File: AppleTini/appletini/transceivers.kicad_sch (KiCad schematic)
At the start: 22 parts, among them U2 74LS245, U3 74LS245, U4 74LS245, U5 74LS245, U5 74LVC1G07, U6 74LVC1G07, U7 74LVC1G07, U8 74LVC1G07, U9 74LS245

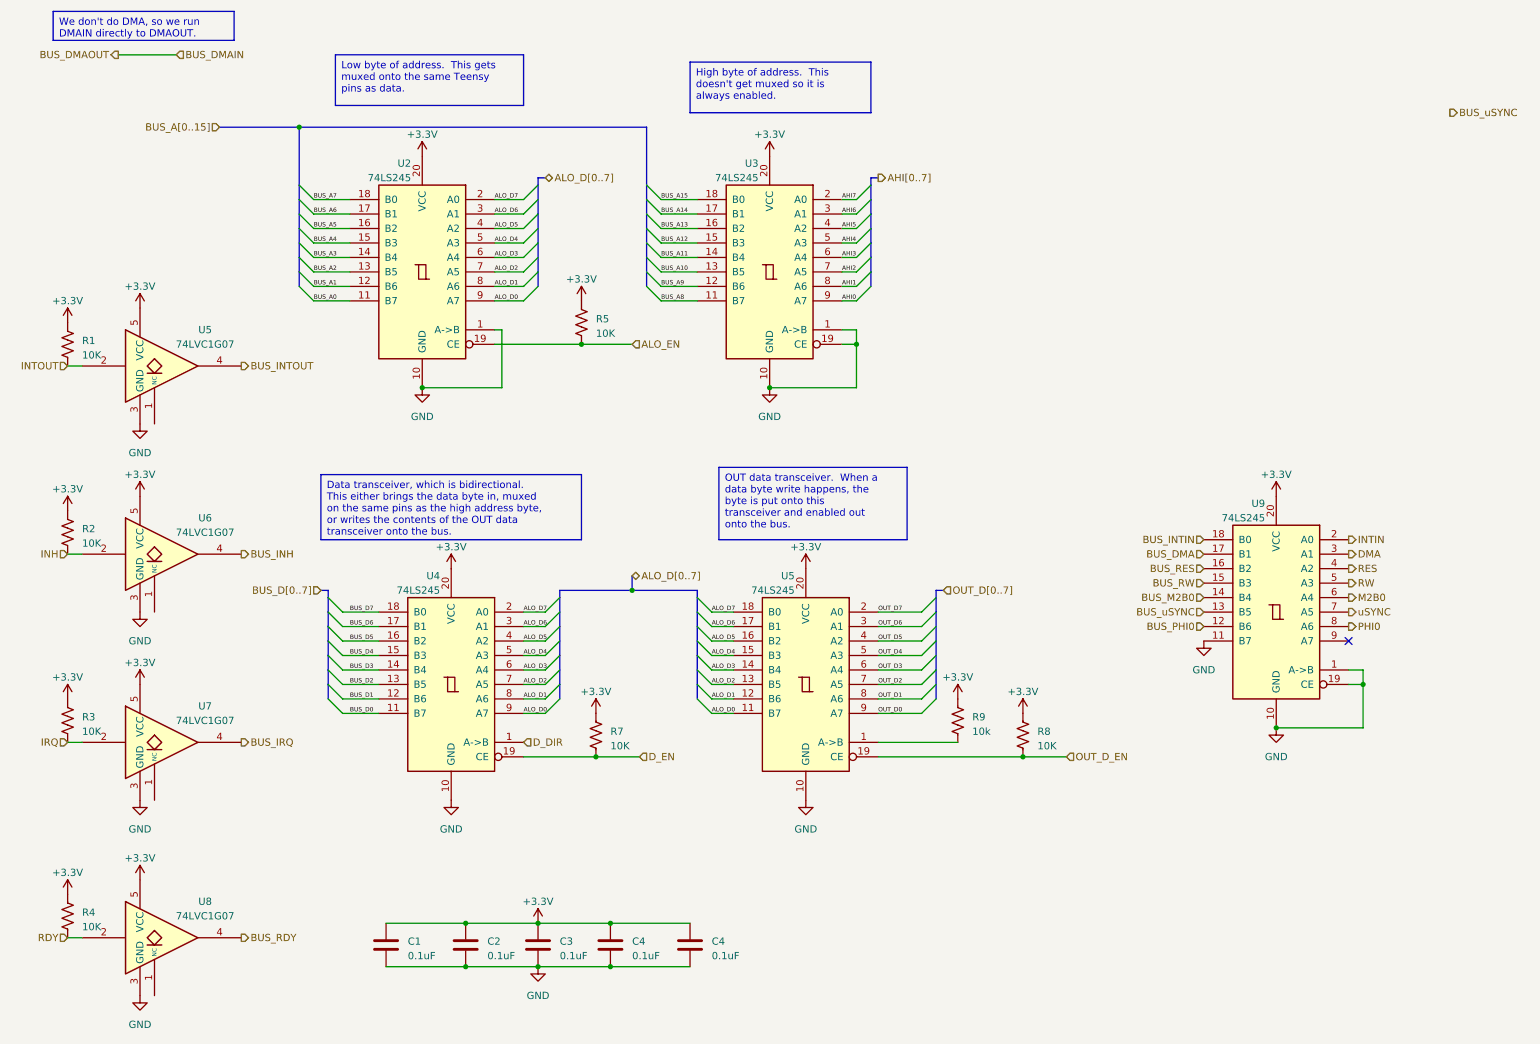
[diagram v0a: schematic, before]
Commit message: Changed to use single LVC07 Shrink vias to 0.6mm Spaced vias further apart Increased zone fill
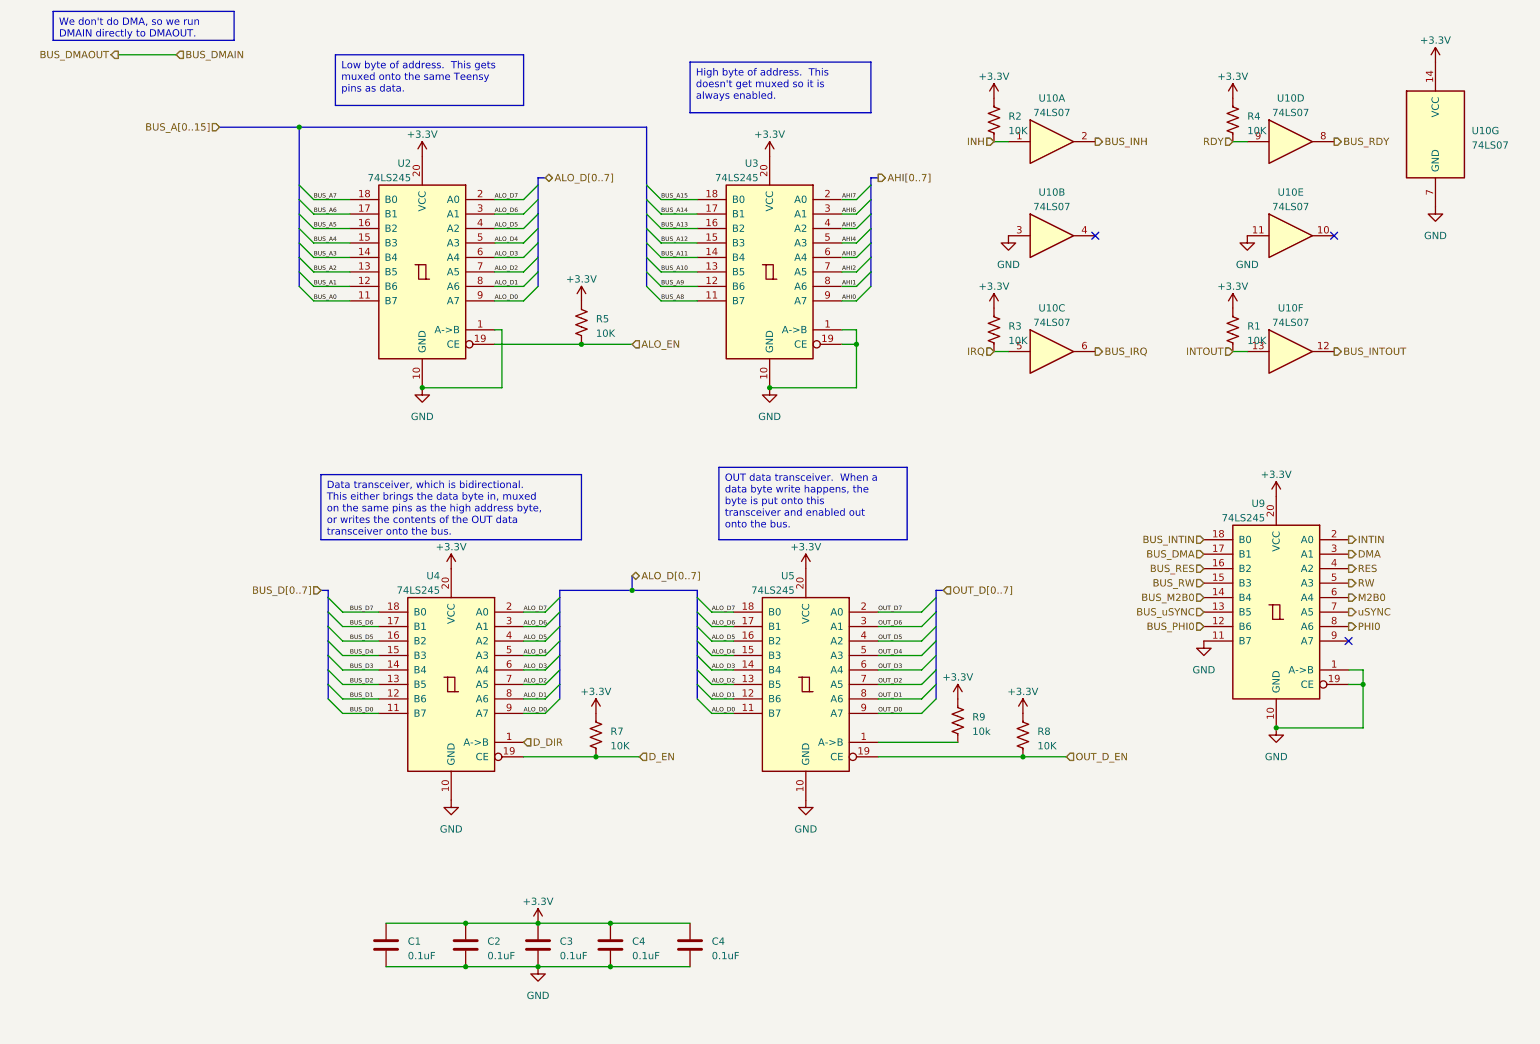
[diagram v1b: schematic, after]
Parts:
- removed U5, U6, U7, U8: 74LVC1G07, Package_TO_SOT_SMD:SOT-23-5, symbol 74xGxx:74LVC1G07
- added U10: 74LS07, Package_SO:TSSOP-14_4.4x5mm_P0.65mm, symbol 74xx:74LS07
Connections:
- net +3.3V: now also U10.14 (VCC)
- net BUS_INH: now also U10.2
- net BUS_INTOUT: now also U10.12
- net BUS_IRQ: now also U10.6
- net BUS_RDY: now also U10.8
- net GND: now also U10.11, U10.3, U10.7 (GND)
- net INH: now also U10.1
- net INTOUT: now also U10.13
- net IRQ: now also U10.5
- net RDY: now also U10.9
- no-connect marks 1 -> 3

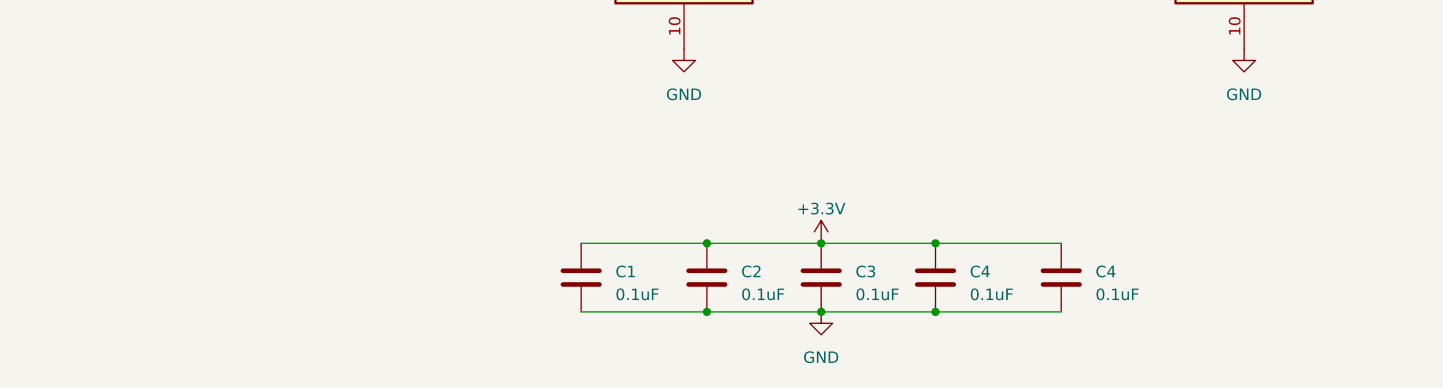
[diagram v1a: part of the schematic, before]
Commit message: Caps on bus power lines
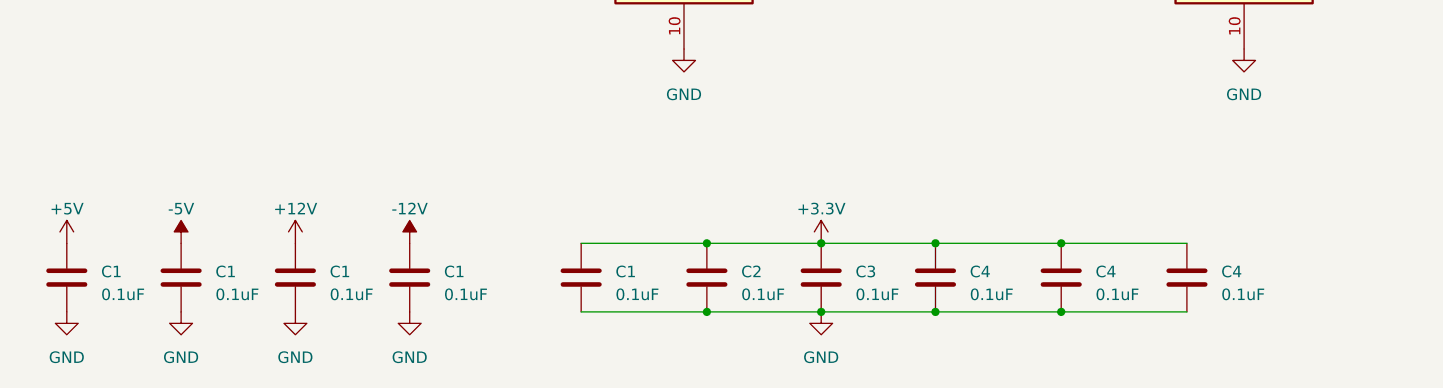
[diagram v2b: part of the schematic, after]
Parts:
- added C1 (x4), C4: 0.1uF, Capacitor_SMD:C_1206_3216Metric, symbol Device:C
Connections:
- net +3.3V: now also C4.1
- net GND: now also C1.2, C1.2, C1.2, C1.2, C4.2
- new net +12V: C1.1
- new net +5V: C1.1
- new net -12V: C1.1
- new net -5V: C1.1

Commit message: part picks and cleanup
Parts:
- C1, C2, C3, C4: LCSC (none) -> C24497
- R1, R2, R3, R4, R5, R7, R8: LCSC (none) -> C2991755
- R9: value 10k -> 10K; LCSC (none) -> C2991755
- U10: LCSC (none) -> C7809
- U2, U3, U4, U5, U9: LCSC (none) -> C6082
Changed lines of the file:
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@@
+      (effects (font (size 1.27 1.27)) hide)
+    )
+    (property "LCSC" "C7809" (at 240.03 74.93 0)
       (effects (font (size 1.27 1.27)) hide)
     )
@@
       (effects (font (size 1.27 1.27)) hide)
     )
+    (property "LCSC" "C6082" (at 154.94 133.35 0)
+      (effects (font (size 1.27 1.27)) hide)
+    )
     (pin "1")
     (pin "10")
@@
       (effects (font (size 1.27 1.27)) hide)
     )
+    (property "LCSC" "C2991755" (at 118.11 142.24 0)
+      (effects (font (size 1.27 1.27)) hide)
+    )
     (pin "1")
     (pin "2")
@@
     )
     (property "Datasheet" "http://www.ti.com/lit/gpn/sn74LS245" (at 92.71 133.35 0)
+      (effects (font (size 1.27 1.27)) hide)
+    )
+    (property "LCSC" "C6082" (at 92.71 133.35 0)
       (effects (font (size 1.27 1.27)) hide)
     )
@@
       (effects (font (size 1.27 1.27)) hide)
     )
+    (property "LCSC" "C6082" (at 237.49 120.65 0)
+      (effects (font (size 1.27 1.27)) hide)
+    )
     (pin "1")
     (pin "10")
@@
       (effects (font (size 1.27 1.27)) hide)
     )
+    (property "LCSC" "C24497" (at 148.59 179.07 0)
+      (effects (font (size 1.27 1.27)) hide)
+    )
     (pin "1")
     (pin "2")
@@
       (effects (font (size 1.27 1.27)) hide)
     )
+    (property "LCSC" "C24497" (at 62.23 179.07 0)
+      (effects (font (size 1.27 1.27)) hide)
+    )
     (pin "1")
     (pin "2")
@@
     )
     (property "Datasheet" "www.ti.com/lit/ds/symlink/sn74ls07.pdf" (at 240.03 54.61 0)
+      (effects (font (size 1.27 1.27)) hide)
+    )
+    (property "LCSC" "C7809" (at 240.03 54.61 0)
       (effects (font (size 1.27 1.27)) hide)
     )
@@
       (effects (font (size 1.27 1.27)) hide)
     )
+    (property "LCSC" "C24497" (at 24.13 179.07 0)
+      (effects (font (size 1.27 1.27)) hide)
+    )
     (pin "1")
     (pin "2")
@@
     )
     (property "Datasheet" "~" (at 229.87 34.29 0)
+      (effects (font (size 1.27 1.27)) hide)
+    )
+    (property "LCSC" "C2991755" (at 229.87 34.29 0)
       (effects (font (size 1.27 1.27)) hide)
     )
@@
     )
     (property "Datasheet" "http://www.ti.com/lit/gpn/sn74LS245" (at 148.59 60.96 0)
+      (effects (font (size 1.27 1.27)) hide)
+    )
+    (property "LCSC" "C6082" (at 148.59 60.96 0)
       (effects (font (size 1.27 1.27)) hide)
     )
@@
       (effects (font (size 1.27 1.27)) hide)
     )
+    (property "LCSC" "C24497" (at 107.95 179.07 0)
+      (effects (font (size 1.27 1.27)) hide)
+    )
     (pin "1")
     (pin "2")
@@
       (effects (font (size 1.27 1.27)) hide)
     )
+    (property "LCSC" "C24497" (at 81.28 179.07 0)
+      (effects (font (size 1.27 1.27)) hide)
+    )
     (pin "1")
     (pin "2")
@@
       (effects (font (size 1.27 1.27)) hide)
     )
+    (property "LCSC" "C2991755" (at 115.57 69.85 0)
+      (effects (font (size 1.27 1.27)) hide)
+    )
     (pin "1")
     (pin "2")
@@
       (effects (font (size 1.27 1.27)) (justify left))
     )
-    (property "Value" "10k" (at 184.15 141.605 0)
+    (property "Value" "10K" (at 184.15 141.605 0)
       (effects (font (size 1.27 1.27)) (justify left))
     )
@@
       (effects (font (size 1.27 1.27)) hide)
     )
+    (property "LCSC" "C2991755" (at 181.61 139.7 0)
+      (effects (font (size 1.27 1.27)) hide)
+    )
     (pin "1")
     (pin "2")
@@
       (effects (font (size 1.27 1.27)) hide)
     )
+    (property "LCSC" "C24497" (at 36.83 179.07 0)
+      (effects (font (size 1.27 1.27)) hide)
+    )
     (pin "1")
     (pin "2")
@@
       (effects (font (size 1.27 1.27)) hide)
     )
+    (property "LCSC" "C24497" (at 120.65 179.07 0)
+      (effects (font (size 1.27 1.27)) hide)
+    )
     (pin "1")
     (pin "2")
@@
       (effects (font (size 1.27 1.27)) hide)
     )
+    (property "LCSC" "C2991755" (at 187.96 34.29 0)
+      (effects (font (size 1.27 1.27)) hide)
+    )
     (pin "1")
     (pin "2")
@@
       (effects (font (size 1.27 1.27)) hide)
     )
+    (property "LCSC" "C24497" (at 134.62 179.07 0)
+      (effects (font (size 1.27 1.27)) hide)
+    )
     (pin "1")
     (pin "2")
@@
     )
     (property "Datasheet" "www.ti.com/lit/ds/symlink/sn74ls07.pdf" (at 198.12 74.93 0)
+      (effects (font (size 1.27 1.27)) hide)
+    )
+    (property "LCSC" "C7809" (at 198.12 74.93 0)
       (effects (font (size 1.27 1.27)) hide)
     )
@@
       (effects (font (size 1.27 1.27)) hide)
     )
+    (property "LCSC" "C24497" (at 95.25 179.07 0)
+      (effects (font (size 1.27 1.27)) hide)
+    )
     (pin "1")
     (pin "2")
@@
       (effects (font (size 1.27 1.27)) hide)
     )
+    (property "LCSC" "C2991755" (at 229.87 71.12 0)
+      (effects (font (size 1.27 1.27)) hide)
+    )
     (pin "1")
     (pin "2")
@@
       (effects (font (size 1.27 1.27)) hide)
     )
+    (property "LCSC" "C2991755" (at 187.96 71.12 0)
+      (effects (font (size 1.27 1.27)) hide)
+    )
     (pin "1")
     (pin "2")
@@
       (effects (font (size 1.27 1.27)) hide)
     )
+    (property "LCSC" "C24497" (at 49.53 179.07 0)
+      (effects (font (size 1.27 1.27)) hide)
+    )
     (pin "1")
     (pin "2")
@@
     )
     (property "Datasheet" "www.ti.com/lit/ds/symlink/sn74ls07.pdf" (at 265.43 36.83 0)
+      (effects (font (size 1.27 1.27)) hide)
+    )
+    (property "LCSC" "C7809" (at 265.43 36.83 0)
       (effects (font (size 1.27 1.27)) hide)
     )
@@
       (effects (font (size 1.27 1.27)) hide)
     )
+    (property "LCSC" "C7809" (at 240.03 38.1 0)
+      (effects (font (size 1.27 1.27)) hide)
+    )
     (pin "1")
     (pin "2")
@@
       (effects (font (size 1.27 1.27)) hide)
     )
+    (property "LCSC" "C7809" (at 198.12 38.1 0)
+      (effects (font (size 1.27 1.27)) hide)
+    )
     (pin "1")
     (pin "2")
@@
       (effects (font (size 1.27 1.27)) hide)
     )
+    (property "LCSC" "C6082" (at 87.63 60.96 0)
+      (effects (font (size 1.27 1.27)) hide)
+    )
     (pin "1")
     (pin "10")
@@
     )
     (property "Datasheet" "www.ti.com/lit/ds/symlink/sn74ls07.pdf" (at 198.12 54.61 0)
+      (effects (font (size 1.27 1.27)) hide)
+    )
+    (property "LCSC" "C7809" (at 198.12 54.61 0)
       (effects (font (size 1.27 1.27)) hide)
     )
@@
       (effects (font (size 1.27 1.27)) hide)
     )
+    (property "LCSC" "C2991755" (at 193.04 142.24 0)
+      (effects (font (size 1.27 1.27)) hide)
+    )

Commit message: 4 layer complete
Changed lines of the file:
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@@
-    (stroke (width 0) (type default))
-  )
-  (wire (pts (xy 34.29 22.86) (xy 44.45 22.86))
     (stroke (width 0) (type default))
   )
@@
     (stroke (width 0) (type default))
   )
-  (text_box "We don't do DMA, so we run DMAIN directly to DMAOUT."
-    (at 22.86 15.24 0) (size 31.75 5.08)
+  (text_box "OUT data transceiver.  When a data byte write happens, the byte is put onto this transceiver and enabled out onto the bus."
+    (at 139.7 95.25 0) (size 33.02 12.7)
     (stroke (width 0) (type default))
     (fill (type none))
     (effects (font (size 1.27 1.27)) (justify left top))
   )
-  (text_box "OUT data transceiver.  When a data byte write happens, the byte is put onto this transceiver and enabled out onto the bus."
-    (at 139.7 95.25 0) (size 33.02 12.7)
+  (text_box "High byte of address.  This doesn't get muxed so it is always enabled."
+    (at 134.62 24.13 0) (size 31.75 8.89)
     (stroke (width 0) (type default))
     (fill (type none))
     (effects (font (size 1.27 1.27)) (justify left top))
   )
-  (text_box "High byte of address.  This doesn't get muxed so it is always enabled."
-    (at 134.62 24.13 0) (size 31.75 8.89)
+  (text_box "Low byte of address.  This gets muxed onto the same Teensy pins as data."
+    (at 72.39 22.86 0) (size 33.02 8.89)
     (stroke (width 0) (type default))
     (fill (type none))
     (effects (font (size 1.27 1.27)) (justify left top))
   )
-  (text_box "Low byte of address.  This gets muxed onto the same Teensy pins as data."
-    (at 72.39 22.86 0) (size 33.02 8.89)
+  (text_box "Data transceiver, which is bidirectional.  This either brings the data byte in, muxed on the same pins as the high address byte, or writes the contents of the OUT data transceiver onto the bus."
+    (at 69.85 96.52 0) (size 45.72 11.43)
     (stroke (width 0) (type default))
     (fill (type none))
     (effects (font (size 1.27 1.27)) (justify left top))
   )
-  (text_box "Data transceiver, which is bidirectional.  This either brings the data byte in, muxed on the same pins as the high address byte, or writes the contents of the OUT data transceiver onto the bus."
-    (at 69.85 96.52 0) (size 45.72 11.43)
-    (stroke (width 0) (type default))
-    (fill (type none))
-    (effects (font (size 1.27 1.27)) (justify left top))
-  )
   (label "ALO_D0" (at 100.33 66.04 0) (fields_autoplaced)
     (effects (font (size 0.762 0.762)) (justify left bottom))
@@
     (effects (font (size 1.27 1.27)) (justify left))
   )
-  (hierarchical_label "BUS_DMAOUT" (shape output) (at 34.29 22.86 180) (fields_autoplaced)
-    (effects (font (size 1.27 1.27)) (justify right))
-  )
   (hierarchical_label "PHI0" (shape output) (at 250.19 123.19 0) (fields_autoplaced)
     (effects (font (size 1.27 1.27)) (justify left))
   )
-  (hierarchical_label "BUS_DMAIN" (shape input) (at 44.45 22.86 0) (fields_autoplaced)
-    (effects (font (size 1.27 1.27)) (justify left))
-  )

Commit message: revisions, passed JLCPCB verification
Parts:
- renumbered R9 to R8, U9 to U5, U10 to U6
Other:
- moved on the sheet: R1, R2, R3, R4, U5, U6A, U6B, U6C, U6D, U6E, U6F, U6G
